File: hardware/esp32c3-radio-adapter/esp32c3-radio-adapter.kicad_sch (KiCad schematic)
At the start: 7 parts, among them J1 Conn_01x08, J2 Conn_01x08, J3 E07-M1101D

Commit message: Merge the two socket adapters into esp32c3-radio-adapter; two-sided pin silk on the replicas
* esp32c3-radio-adapter replaces esp32c3-cc1101-adapter and
  esp32c3-ra02-adapter: the E07-M1101D and Ra-02 breakout headers differ
  only at outer column 3 (GDO0 / RST) and inner column 1 (GDO2 / DIO0),
  wired to GPIO10 and GPIO3, so one socket takes either board.  Nets are
  named GDO0_RST, GDO2_DIO0 and CSN_NSS; the silk carries the E07 names
  with the Ra-02 names in parentheses, plus both boards' fab outlines.
* Ra-02 breakout replica: header and module pin numbers on the back silk;
  header pin names beside each column on both sides.
* E07-M1101D replica: pin names beside each column on both sides; the
  markers, box and legend are mirrored onto the back.
* Pinout diagrams combined into docs/images/pinout-radio-boards.svg.
* README, export defaults and generator lists updated.

Co-Authored-By: Claude Fable 5.1 <noreply@anthropic.com>
Claude-Session: https://claude.ai/code/session_01JoGdh4Cg3VtTTDZi4gQuiN
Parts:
- J3: value E07-M1101D -> E07-M1101D_or_Ra-02
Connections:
- net DIO0 renamed GDO0_RST
- net DIO1 renamed GDO2_DIO0
- net NSS renamed CSN_NSS
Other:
- note added: "ESP32-C3 SuperMini (J1 = GPIO row, J2 = power row; through-hole or castellated) driving a CC1101 E07-M1101D board or an SX1278 Ra-02 breakout in socket J3. SPI: MOSI=GPIO5 SCK=GPIO6 CSN/NSS=GPIO7 MISO=GPIO4; GDO0 (Ra-02: RST)=GPIO10, GDO2 (Ra-02: DIO0)=GPIO3. H1-H4: M2 mounting holes. All tracks on B.Cu; F.Cu carries a GND pour."
- note removed: "ESP32-C3 SuperMini (J1 = GPIO row, J2 = power row; through-hole or castellated) driving a CC1101 E07-M1101D board in socket J3. SPI: MOSI=GPIO5 SCK=GPIO6 CSN=GPIO7 MISO=GPIO4; GDO0=GPIO10 GDO2=GPIO3. H1-H4: M2 mounting holes. All tracks on B.Cu; F.Cu carries a GND pour."
- title: ESP32-C3 SuperMini to CC1101 E07-M1101D adapter -> ESP32-C3 SuperMini to CC1101 (E07-M1101D) or SX1278 Ra-02 breakout adapter
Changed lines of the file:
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@@
 	(paper "A4")
 	(title_block
-		(title "ESP32-C3 SuperMini to CC1101 E07-M1101D adapter")
+		(title "ESP32-C3 SuperMini to CC1101 (E07-M1101D) or SX1278 Ra-02 breakout adapter")
 		(rev "${GIT_DESCRIBE}")
-		(comment 1 "Carrier joining an ESP32-C3 SuperMini to an Ebyte E07-M1101D-SMA CC1101 433MHz board via a 2x4 socket; all tracks on the back, GND pour on the front")
+		(comment 1 "Carrier joining an ESP32-C3 SuperMini to an Ebyte E07-M1101D-SMA CC1101 board or an SX1278 Ra-02 breakout via one 2x4 socket; all tracks on the back, GND pour on the front")
 	)
 	(symbol
@@
 		)
 		(instances
-			(project "esp32c3-cc1101-adapter"
+			(project "esp32c3-radio-adapter"
 				(path "/b71943b6-a88f-5429-bfd6-fb1a52f93b27"
 					(reference "J1")
@@
 		)
 	)
-	(global_label "NSS"
+	(global_label "CSN_NSS"
 		(shape bidirectional)
 		(at 71.12 99.06 180)
@@
 		)
 	)
-	(global_label "DIO0"
+	(global_label "GDO0_RST"
 		(shape bidirectional)
 		(at 71.12 106.68 180)
@@
 		)
 		(instances
-			(project "esp32c3-cc1101-adapter"
+			(project "esp32c3-radio-adapter"
 				(path "/b71943b6-a88f-5429-bfd6-fb1a52f93b27"
 					(reference "J2")
@@
 		)
 	)
-	(global_label "DIO1"
+	(global_label "GDO2_DIO0"
 		(shape bidirectional)
 		(at 96.52 104.14 180)
@@
 			)
 		)
-		(property "Value" "E07-M1101D"
+		(property "Value" "E07-M1101D_or_Ra-02"
 			(at 129.54 114.3 0)
 			(effects
@@
 			)
 		)
-		(property "Description" "CC1101 E07-M1101D socket"
+		(property "Description" "Radio board socket (CC1101 E07-M1101D or SX1278 Ra-02 breakout)"
 			(at 127 101.6 0)
 			(effects
@@
 		)
 		(instances
-			(project "esp32c3-cc1101-adapter"
+			(project "esp32c3-radio-adapter"
 				(path "/b71943b6-a88f-5429-bfd6-fb1a52f93b27"
 					(reference "J3")
@@
 		)
 	)
-	(global_label "DIO0"
+	(global_label "GDO0_RST"
 		(shape bidirectional)
 		(at 121.92 101.6 180)
@@
 		)
 	)
-	(global_label "NSS"
+	(global_label "CSN_NSS"
 		(shape bidirectional)
 		(at 134.62 101.6 0)
@@
 		)
 	)
-	(global_label "DIO1"
+	(global_label "GDO2_DIO0"
 		(shape bidirectional)
 		(at 134.62 106.68 0)
@@
 		)
 		(instances
-			(project "esp32c3-cc1101-adapter"
+			(project "esp32c3-radio-adapter"
 				(path "/b71943b6-a88f-5429-bfd6-fb1a52f93b27"
 					(reference "H1")
@@
 		)
 		(instances
-			(project "esp32c3-cc1101-adapter"
+			(project "esp32c3-radio-adapter"
 				(path "/b71943b6-a88f-5429-bfd6-fb1a52f93b27"
 					(reference "H2")
@@
 		)
 		(instances
-			(project "esp32c3-cc1101-adapter"
+			(project "esp32c3-radio-adapter"
 				(path "/b71943b6-a88f-5429-bfd6-fb1a52f93b27"
 					(reference "H3")
@@
 		)
 		(instances
-			(project "esp32c3-cc1101-adapter"
+			(project "esp32c3-radio-adapter"
 				(path "/b71943b6-a88f-5429-bfd6-fb1a52f93b27"
 					(reference "H4")
@@
 		)
 	)
-	(text "ESP32-C3 SuperMini (J1 = GPIO row, J2 = power row; through-hole or castellated) driving a CC1101 E07-M1101D board in socket J3.\nSPI: MOSI=GPIO5 SCK=GPIO6 CSN=GPIO7 MISO=GPIO4; GDO0=GPIO10 GDO2=GPIO3.\nH1-H4: M2 mounting holes.  All tracks on B.Cu; F.Cu carries a GND pour."
+	(text "ESP32-C3 SuperMini (J1 = GPIO row, J2 = power row; through-hole or castellated) driving a CC1101 E07-M1101D board or an SX1278 Ra-02 breakout in socket J3.\nSPI: MOSI=GPIO5 SCK=GPIO6 CSN/NSS=GPIO7 MISO=GPIO4; GDO0 (Ra-02: RST)=GPIO10, GDO2 (Ra-02: DIO0)=GPIO3.\nH1-H4: M2 mounting holes.  All tracks on B.Cu; F.Cu carries a GND pour."
 		(exclude_from_sim no)
 		(at 60 90 0)

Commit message: Adapters: expansion header for the unused SuperMini pins and a radio-type strap
Pin-header adapter:
* J4, a 1x7 2.54 mm header on the top edge, carries every SuperMini pin the
  radio does not use: 5V, GPIO8, GPIO9, GPIO2, GPIO20, GPIO21, GPIO0.  Its
  pins sit at the gaps between the SuperMini's pins so each net reaches it on
  the front copper without crossing another (power-row nets jog above their
  row, GPIO-row nets rise between the rows and pass between the power-row
  pads).  The radio tracks on the back are unchanged; the GND pour flows
  around the new tracks.
* JP1, a two-pad solder jumper right of the SuperMini, straps GPIO1 (net
  RADIO_ID) to GND: open = CC1101 E07-M1101D, bridged = Ra-02 breakout.

SX1278 module adapter: GPIO1 is tied to 3V3 (silk "ID=3V3"), so the same
pin reads high there.  Firmware samples GPIO1 with the internal pull-down
and then the pull-up to tell the three states apart; GPIO1 is not a boot
strapping pin.

The header is 2.3 mm from the top edge so the MISO lane on the back keeps
its clearance under it.  Both adapters pass ERC and DRC; README and the
manufacturing notes describe the header and the strap.

Co-Authored-By: Claude Fable 5.1 <noreply@anthropic.com>
Claude-Session: https://claude.ai/code/session_01JoGdh4Cg3VtTTDZi4gQuiN
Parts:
- added J4: Expansion, Adapter:PinHeader_1x07_P2.54mm_Vertical, symbol Connector_Generic:Conn_01x07
- added JP1: RA-02, Adapter:SolderJumper-2_P1.3mm_Open_Pad1.2x1.0mm, symbol Jumper:SolderJumper_2_Open
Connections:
- net +5V: now also J4.1 (Pin_1)
- net GND: now also JP1.2 (B)
- net GPIO0: now also J4.7 (Pin_7)
- net GPIO2: now also J4.4 (Pin_4)
- net GPIO20: now also J4.5 (Pin_5)
- net GPIO21: now also J4.6 (Pin_6)
- net GPIO8: now also J4.2 (Pin_2)
- net GPIO9: now also J4.3 (Pin_3)
- net GPIO1 renamed RADIO_ID
- net RADIO_ID: now also JP1.1 (A)
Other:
- note added: "ESP32-C3 SuperMini (J1 = GPIO row, J2 = power row; through-hole or castellated) driving a CC1101 E07-M1101D board or an SX1278 Ra-02 breakout in socket J3. SPI: MOSI=GPIO5 SCK=GPIO6 CSN/NSS=GPIO7 MISO=GPIO4; GDO0 (Ra-02: RST)=GPIO10, GDO2 (Ra-02: DIO0)=GPIO3. J4: the unused SuperMini pins. JP1: radio-type strap on GPIO1 (RADIO_ID), open = CC1101, bridged to GND = Ra-02. H1-H4: M2 mounting holes. 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"
- note removed: "ESP32-C3 SuperMini (J1 = GPIO row, J2 = power row; through-hole or castellated) driving a CC1101 E07-M1101D board or an SX1278 Ra-02 breakout in socket J3. SPI: MOSI=GPIO5 SCK=GPIO6 CSN/NSS=GPIO7 MISO=GPIO4; GDO0 (Ra-02: RST)=GPIO10, GDO2 (Ra-02: DIO0)=GPIO3. H1-H4: M2 mounting holes. All tracks on B.Cu; F.Cu carries a GND pour."

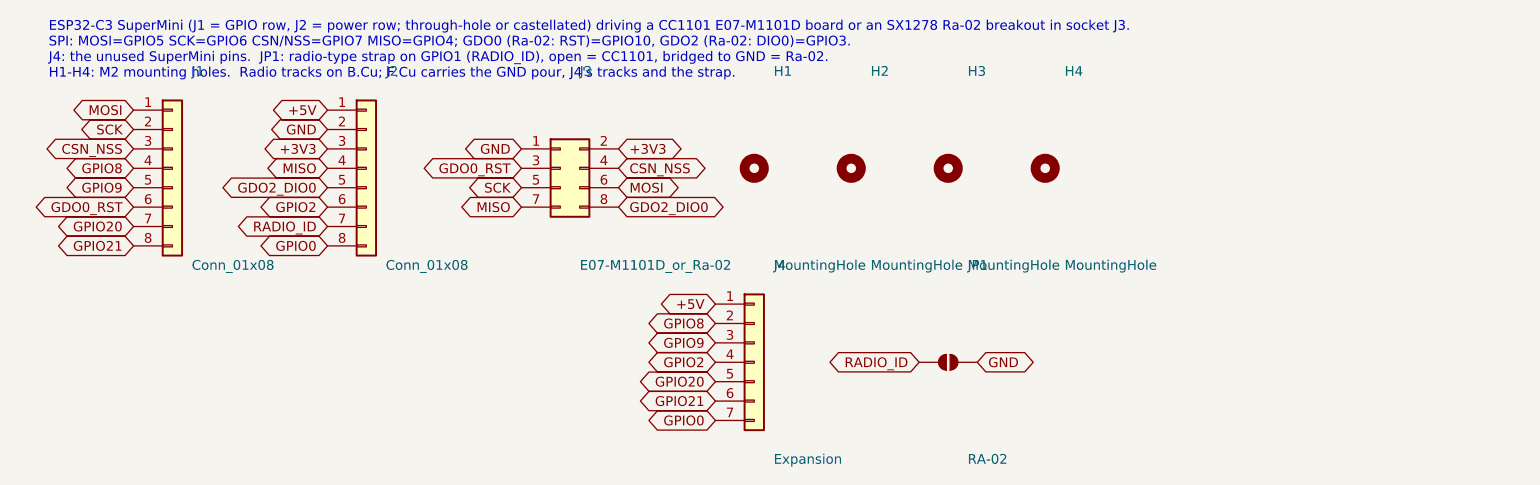
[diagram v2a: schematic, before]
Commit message: Radio adapter: strap as a jumper header plus 0805 resistor; expansion header centred
* JP1 is now a 1x2 2.54 mm header for an ordinary jumper, with R1 (0805 pads,
  0R) in parallel as the permanent alternative; both take RADIO_ID (GPIO1)
  to GND.  They sit on the front beside the socket, past the SuperMini's
  antenna end so a jumper cap clears it, and right of the MISO/GDO2 descents
  on the back, which widens the board to 29 x 36.5 mm.
* J4 (the unused-pin header) is centred between the top mounting holes, its
  pin order now 5V, 8, 9, 2, 20, 0, 21.  RADIO_ID leaves the power row
  downward through the gap between GPIO-row pins 7 and 8 and runs under
  that row to JP1; GPIO21 goes round the right of the SuperMini to the last
  header pin, so the front routes still do not cross.

Co-Authored-By: Claude Fable 5.1 <noreply@anthropic.com>
Claude-Session: https://claude.ai/code/session_01JoGdh4Cg3VtTTDZi4gQuiN
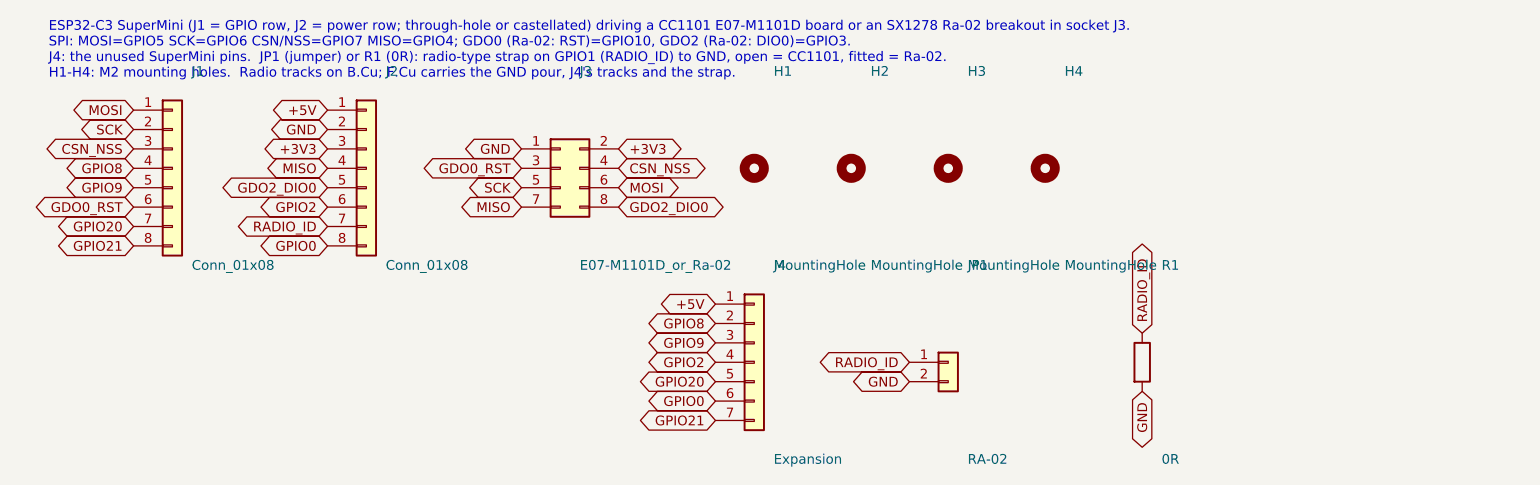
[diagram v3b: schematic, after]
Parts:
- added R1: 0R, Adapter:R_0805_2012Metric_HandSolder_AlongY, symbol Device:R
- JP1: footprint Adapter:SolderJumper-2_P1.3mm_Open_Pad1.2x1.0mm -> Adapter:PinHeader_1x02_P2.54mm_Vertical_AlongY; symbol Jumper:SolderJumper_2_Open -> Connector_Generic:Conn_01x02
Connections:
- net GND: now also R1.2
- net GPIO0: now also J4.6 (Pin_6); no longer J4.7 (Pin_7)
- net GPIO21: now also J4.7 (Pin_7); no longer J4.6 (Pin_6)
- net RADIO_ID: now also R1.1
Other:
- note added: "ESP32-C3 SuperMini (J1 = GPIO row, J2 = power row; through-hole or castellated) driving a CC1101 E07-M1101D board or an SX1278 Ra-02 breakout in socket J3. SPI: MOSI=GPIO5 SCK=GPIO6 CSN/NSS=GPIO7 MISO=GPIO4; GDO0 (Ra-02: RST)=GPIO10, GDO2 (Ra-02: DIO0)=GPIO3. J4: the unused SuperMini pins. JP1 (jumper) or R1 (0R): radio-type strap on GPIO1 (RADIO_ID) to GND, open = CC1101, fitted = Ra-02. H1-H4: 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"
- note removed: "ESP32-C3 SuperMini (J1 = GPIO row, J2 = power row; through-hole or castellated) driving a CC1101 E07-M1101D board or an SX1278 Ra-02 breakout in socket J3. SPI: MOSI=GPIO5 SCK=GPIO6 CSN/NSS=GPIO7 MISO=GPIO4; GDO0 (Ra-02: RST)=GPIO10, GDO2 (Ra-02: DIO0)=GPIO3. J4: the unused SuperMini pins. JP1: radio-type strap on GPIO1 (RADIO_ID), open = CC1101, bridged to GND = Ra-02. H1-H4: M2 mounting holes. 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"
- moved on the sheet: JP1
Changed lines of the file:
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@@
 		)
 	)
-	(global_label "GPIO21"
+	(global_label "GPIO0"
 		(shape bidirectional)
 		(at 147.32 132.08 180)
@@
 		)
 	)
-	(global_label "GPIO0"
+	(global_label "GPIO21"
 		(shape bidirectional)
 		(at 147.32 134.62 180)
@@
 	)
 	(symbol
-		(lib_id "Jumper:SolderJumper_2_Open")
+		(lib_id "Connector_Generic:Conn_01x02")
 		(at 177.8 127 0)
 		(unit 1)
@@
 			)
 		)
-		(property "Footprint" "Adapter:SolderJumper-2_P1.3mm_Open_Pad1.2x1.0mm"
+		(property "Footprint" "Adapter:PinHeader_1x02_P2.54mm_Vertical_AlongY"
 			(at 177.8 127 0)
 			(effects
@@
 			)
 		)
-		(property "Description" "Radio-type strap: bridge for the Ra-02 breakout, leave open for the CC1101"
+		(property "Description" "Radio-type strap: fit a jumper for the Ra-02 breakout, leave open for the CC1101"
 			(at 177.8 127 0)
 			(effects
@@
 	(global_label "RADIO_ID"
 		(shape bidirectional)
-		(at 173.99 127 180)
+		(at 172.72 127 180)
 		(fields_autoplaced yes)
 		(effects
@@
 		)
 		(property "Intersheetrefs" "${INTERSHEET_REFS}"
-			(at 173.99 127 0)
+			(at 172.72 127 0)
 			(effects
 				(font
@@
 	(global_label "GND"
 		(shape bidirectional)
-		(at 181.61 127 0)
+		(at 172.72 129.54 180)
 		(fields_autoplaced yes)
 		(effects
@@
 				(size 1.27 1.27)
 			)
+			(justify right)
+		)
+		(property "Intersheetrefs" "${INTERSHEET_REFS}"
+			(at 172.72 129.54 0)
+			(effects
+				(font
+					(size 1.27 1.27)
+				)
+				(justify right)
+				(hide yes)
+			)
+		)
+	)
+	(symbol
+		(lib_id "Device:R")
+		(at 203.2 127 0)
+		(unit 1)
+		(exclude_from_sim no)
+		(in_bom yes)
+		(on_board yes)
+		(dnp no)
+		(fields_autoplaced yes)
+		(property "Reference" "R1"
+			(at 205.74 114.3 0)
+			(effects
+				(font
+					(size 1.27 1.27)
+				)
+				(justify left)
+			)
+		)
+		(property "Value" "0R"
+			(at 205.74 139.7 0)
+			(effects
+				(font
+					(size 1.27 1.27)
+				)
+				(justify left)
+			)
+		)
+		(property "Footprint" "Adapter:R_0805_2012Metric_HandSolder_AlongY"
+			(at 203.2 127 0)
+			(effects
+				(font
+					(size 1.27 1.27)
+				)
+				(hide yes)
+			)
+		)
+		(property "Datasheet" "~"
+			(at 203.2 127 0)
+			(effects
+				(font
+					(size 1.27 1.27)
+				)
+				(hide yes)
+			)
+		)
+		(property "Description" "Radio-type strap, alternative to JP1: fit 0R for the Ra-02 breakout"
+			(at 203.2 127 0)
+			(effects
+				(font
+					(size 1.27 1.27)
+				)
+				(hide yes)
+			)
+		)
+		(pin "1"
+		)
+		(pin "2"
+		)
+		(instances
+			(project "esp32c3-radio-adapter"
+				(path "/b71943b6-a88f-5429-bfd6-fb1a52f93b27"
+					(reference "R1")
+					(unit 1)
+				)
+			)
+		)
+	)
+	(global_label "RADIO_ID"
+		(shape bidirectional)
+		(at 203.2 123.19 90)
+		(fields_autoplaced yes)
+		(effects
+			(font
+				(size 1.27 1.27)
+			)
 			(justify left)
 		)
 		(property "Intersheetrefs" "${INTERSHEET_REFS}"
-			(at 181.61 127 0)
-			(effects
-				(font
-					(size 1.27 1.27)
-				)
-				(justify left)
+			(at 203.2 123.19 0)
+			(effects
+				(font
+					(size 1.27 1.27)
+				)
+				(justify left)
+				(hide yes)
+			)
+		)
+	)
+	(global_label "GND"
+		(shape bidirectional)
+		(at 203.2 130.81 270)
+		(fields_autoplaced yes)
+		(effects
+			(font
+				(size 1.27 1.27)
+			)
+			(justify right)
+		)
+		(property "Intersheetrefs" "${INTERSHEET_REFS}"
+			(at 203.2 130.81 0)
+			(effects
+				(font
+					(size 1.27 1.27)
+				)
+				(justify right)
 				(hide yes)
 			)
@@
 		)
 	)
-	(text "ESP32-C3 SuperMini (J1 = GPIO row, J2 = power row; through-hole or castellated) driving a CC1101 E07-M1101D board or an SX1278 Ra-02 breakout in socket J3.\nSPI: MOSI=GPIO5 SCK=GPIO6 CSN/NSS=GPIO7 MISO=GPIO4; GDO0 (Ra-02: RST)=GPIO10, GDO2 (Ra-02: DIO0)=GPIO3.\nJ4: the unused SuperMini pins.  JP1: radio-type strap on GPIO1 (RADIO_ID), open = CC1101, bridged to GND = Ra-02.\nH1-H4: M2 mounting holes.  Radio tracks on B.Cu; F.Cu carries the GND pour, J4's tracks and the strap."
+	(text "ESP32-C3 SuperMini (J1 = GPIO row, J2 = power row; through-hole or castellated) driving a CC1101 E07-M1101D board or an SX1278 Ra-02 breakout in socket J3.\nSPI: MOSI=GPIO5 SCK=GPIO6 CSN/NSS=GPIO7 MISO=GPIO4; GDO0 (Ra-02: RST)=GPIO10, GDO2 (Ra-02: DIO0)=GPIO3.\nJ4: the unused SuperMini pins.  JP1 (jumper) or R1 (0R): radio-type strap on GPIO1 (RADIO_ID) to GND, open = CC1101, fitted = Ra-02.\nH1-H4: M2 mounting holes.  Radio tracks on B.Cu; F.Cu carries the GND pour, J4's tracks and the strap."
 		(exclude_from_sim no)
 		(at 60 90 0)
